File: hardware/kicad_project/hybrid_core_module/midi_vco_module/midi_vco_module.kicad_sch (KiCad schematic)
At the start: 14 parts, among them J1 AudioJack2_SwitchT, J2 Screw_Terminal_01x08, J3 AudioJack2_SwitchT, J4 AudioJack2_SwitchT, J5 AudioJack2_SwitchT, J6 AudioJack2_SwitchT, SW1 SW_Push, SW2 SW_Rotary_1x4_MP, SW3 SW_Rotary_1x4_MP

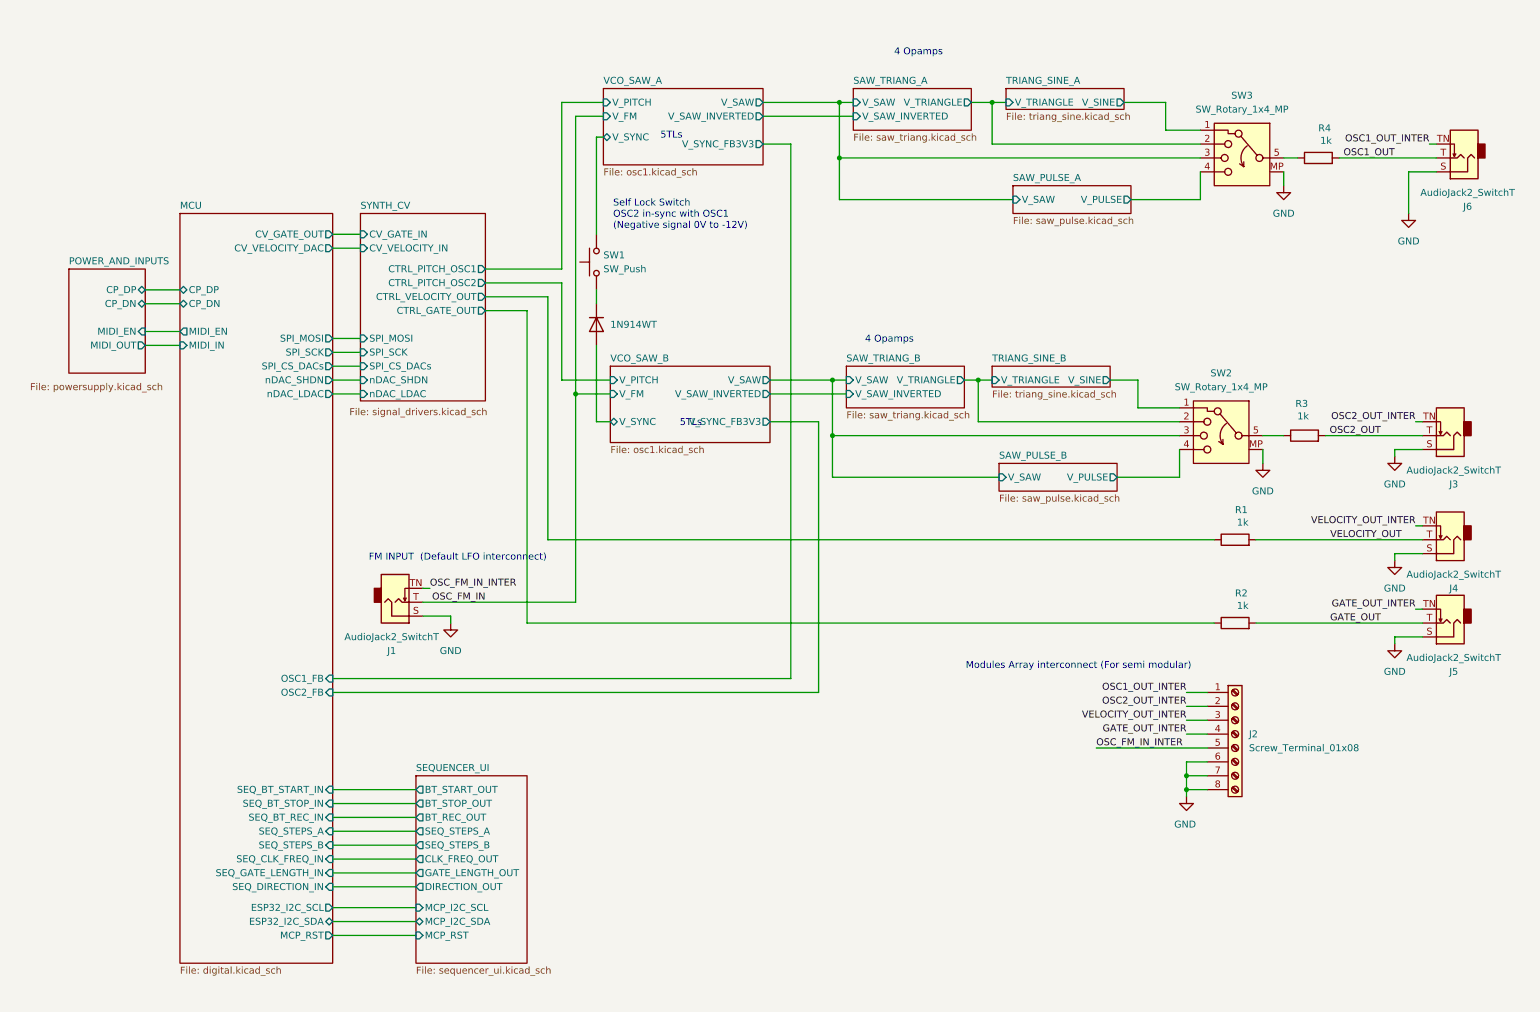
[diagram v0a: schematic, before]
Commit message: Schematic updated. Components Footprint assignment started. Waiting for components mechanical validation before starting layout.
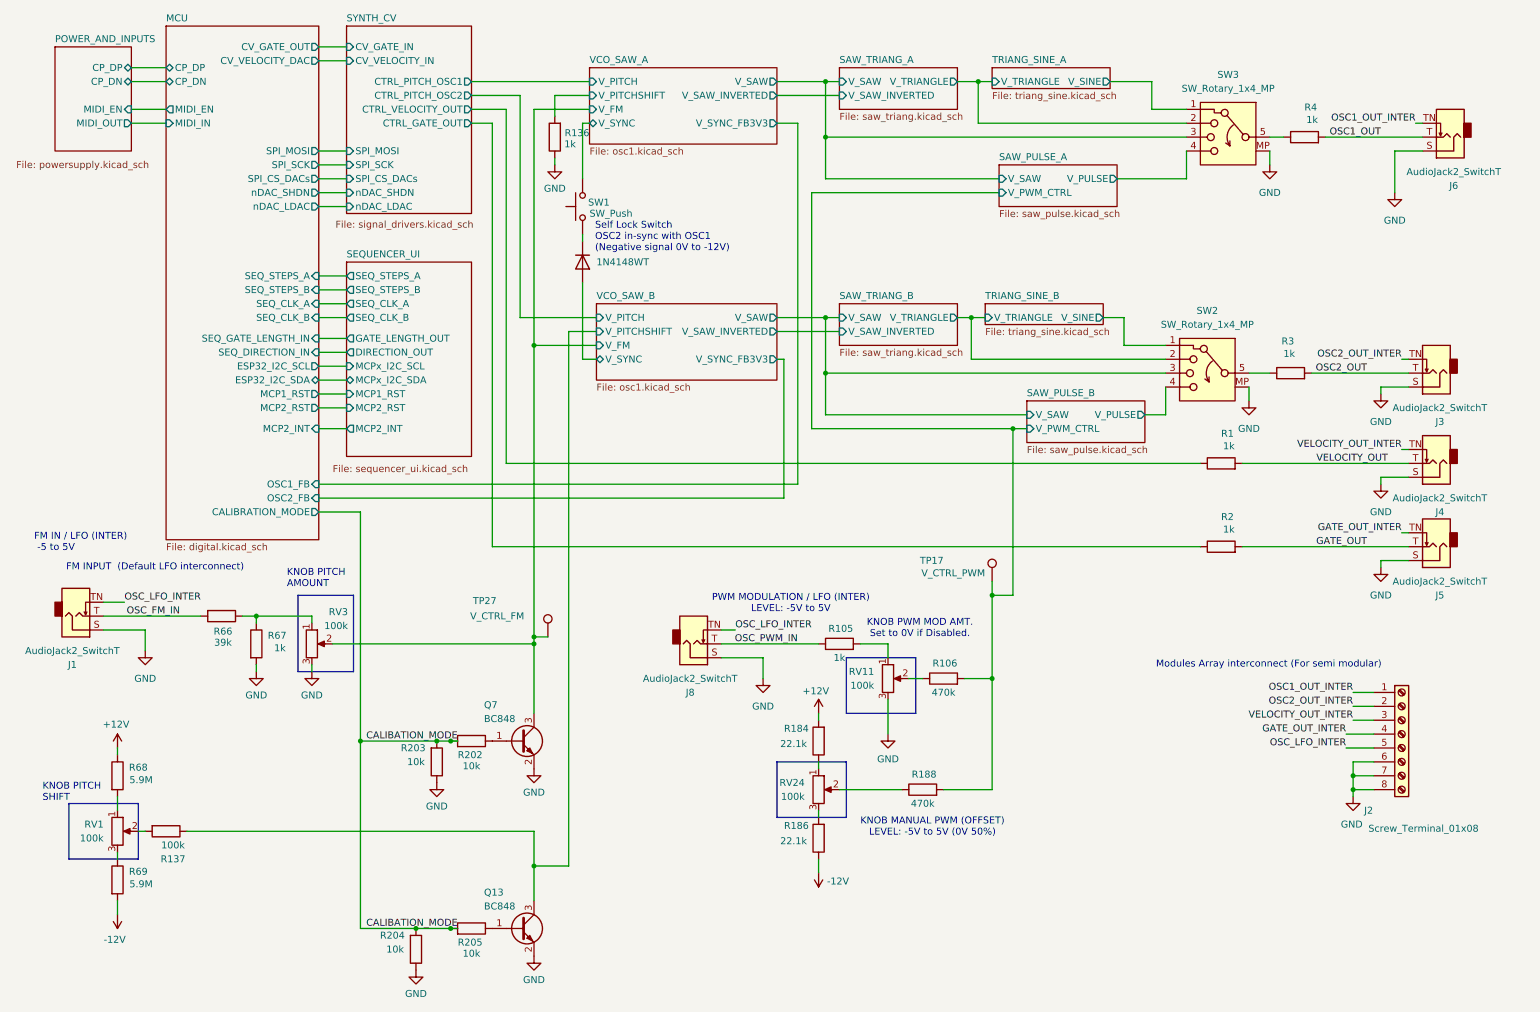
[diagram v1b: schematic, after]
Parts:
- added J8: AudioJack2_SwitchT, mylib:Jack_3.5mm_QingPu_WQP-PJ398SM_Vertical_CircularHoles, symbol Connector_Audio:AudioJack2_SwitchT
- added Q13, Q7: BC848, Package_TO_SOT_SMD:SOT-23, symbol Transistor_BJT:BC848
- added R105, R136, R67: 1k, Resistor_SMD:R_0402_1005Metric, symbol Device:R
- added R106, R188: 470k, Resistor_SMD:R_0402_1005Metric, symbol Device:R
- added R137: 100k, Resistor_SMD:R_0402_1005Metric, symbol Device:R
- added R184, R186: 22.1k, Resistor_SMD:R_0402_1005Metric, symbol Device:R
- added R202, R203, R204, R205: 10k, Resistor_SMD:R_0402_1005Metric, symbol Device:R
- added R66: 39k, Resistor_SMD:R_0402_1005Metric, symbol Device:R
- added R68, R69: 5.9M, Resistor_SMD:R_0402_1005Metric, symbol Device:R
- added RV1, RV11, RV24, RV3: 100k, symbol Device:R_Potentiometer
- added TP17: V_CTRL_PWM, symbol Connector:TestPoint
- added TP27: V_CTRL_FM, symbol Connector:TestPoint
- D1: value 1N914WT -> 1N4148WT; Manufacturer (none) -> ONSEMI/FAIRCHILD; Manufacturer PartNumer (none) -> 1N4148WT
- J1, J3, J4, J5, J6: footprint (none) -> mylib:Jack_3.5mm_QingPu_WQP-PJ398SM_Vertical_CircularHoles
- J2: footprint (none) -> TerminalBlock_CUI:TerminalBlock_CUI_TB007-508-08_1x08_P5.08mm_Horizontal; Manufacturer (none) -> Same Sky; Manufacturer PartNumer (none) -> TB007-508-08BE
- R1, R2, R3, R4: footprint (none) -> Resistor_SMD:R_0402_1005Metric; Manufacturer (none) -> YAGEO; Manufacturer PartNumer (none) -> RT0402FRE071KL
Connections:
- net GND: now also J8.S, Q13.2 (E), Q7.2 (E), R136.1, R203.1, R204.1, R67.2, RV11.3, RV3.3
- net OSC_FM_IN: now also R66.2
- net OSC_FM_IN_INTER renamed OSC_LFO_INTER
- net OSC_LFO_INTER: now also J8.TN
- new net: R186.2, RV24.3
- new net: R105.2, RV11.1
- new net: R106.1, RV11.2
- new net: R66.1, R67.1, RV3.1
- new net: R184.1, RV24.1
- new net: Q7.1 (B), R202.1
- new net: R68.2, RV1.1
- new net: R69.1, RV1.3
- new net: R137.2, RV1.2
- new net: Q13.1 (B), R205.1
- new net: R188.1, RV24.2
- new net +12V: R184.2, R68.1
- new net -12V: R186.1, R69.2
- new net CALIBATION_MODE: R202.2, R203.2, R204.2, R205.2
- new net OSC_PWM_IN: J8.T, R105.1
- new net SAW_PULSE_A/V_PWM_CTRL: R106.2, R188.2, TP17.1
- new net VCO_SAW_A/V_FM: Q7.3 (C), RV3.2, TP27.1
- new net VCO_SAW_A/V_PITCHSHIFT: R136.2
- new net VCO_SAW_B/V_PITCHSHIFT: Q13.3 (C), R137.1
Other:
- sheet MCU ports: added CALIBRATION_MODE, MCP1_RST, MCP2_INT, MCP2_RST, SEQ_CLK_A, SEQ_CLK_B; removed MCP_RST, SEQ_BT_REC_IN, SEQ_BT_START_IN, SEQ_BT_STOP_IN, SEQ_CLK_FREQ_IN
- sheet SAW_PULSE_A ports: added V_PWM_CTRL; removed none
- sheet SAW_PULSE_B ports: added V_PWM_CTRL; removed none
- sheet SEQUENCER_UI ports: added MCP1_RST, MCP2_INT, MCP2_RST, MCPx_I2C_SCL, MCPx_I2C_SDA, SEQ_CLK_A, SEQ_CLK_B; removed BT_REC_OUT, BT_START_OUT, BT_STOP_OUT, CLK_FREQ_OUT, MCP_I2C_SCL, MCP_I2C_SDA, MCP_RST
- sheet VCO_SAW_A ports: added V_PITCHSHIFT; removed none
- sheet VCO_SAW_B ports: added V_PITCHSHIFT; removed none
- note added: "FM IN / LFO (INTER) -5 to 5V"
- note added: "KNOB MANUAL PWM (OFFSET) LEVEL: -5V to 5V (0V 50%)"
- note added: "KNOB PITCH AMOUNT"
- note added: "KNOB PITCH SHIFT"
- note added: "KNOB PWM MOD AMT. Set to 0V if Disabled."
- note added: "PWM MODULATION / LFO (INTER) LEVEL: -5V to 5V"
- note removed: "4 Opamps"
- note removed: "5TLs"
- moved on the sheet: J1, J2, J3, J4, J5, J6, R1, R2, R3, R4, SW1, SW2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

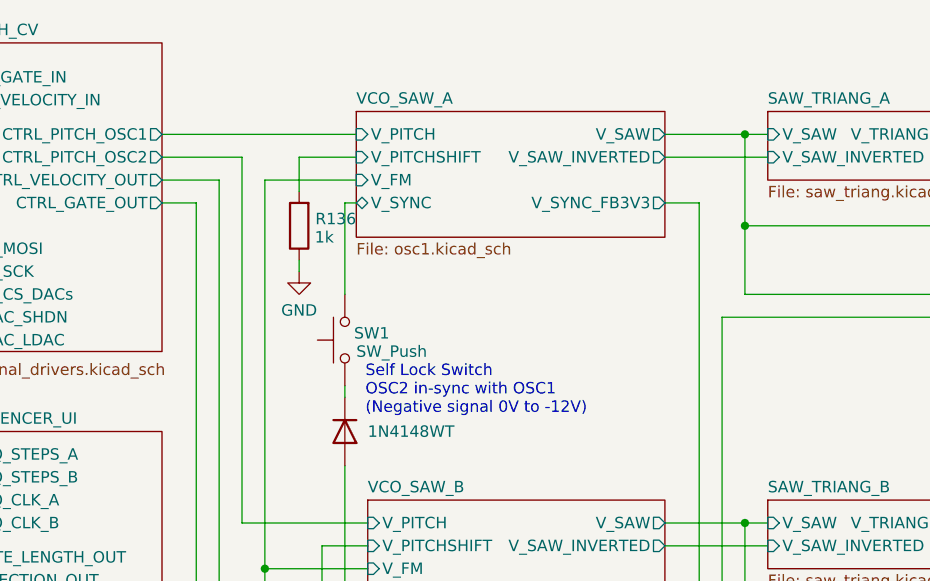
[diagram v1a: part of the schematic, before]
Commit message: - schematic updated  - PN and footprints added
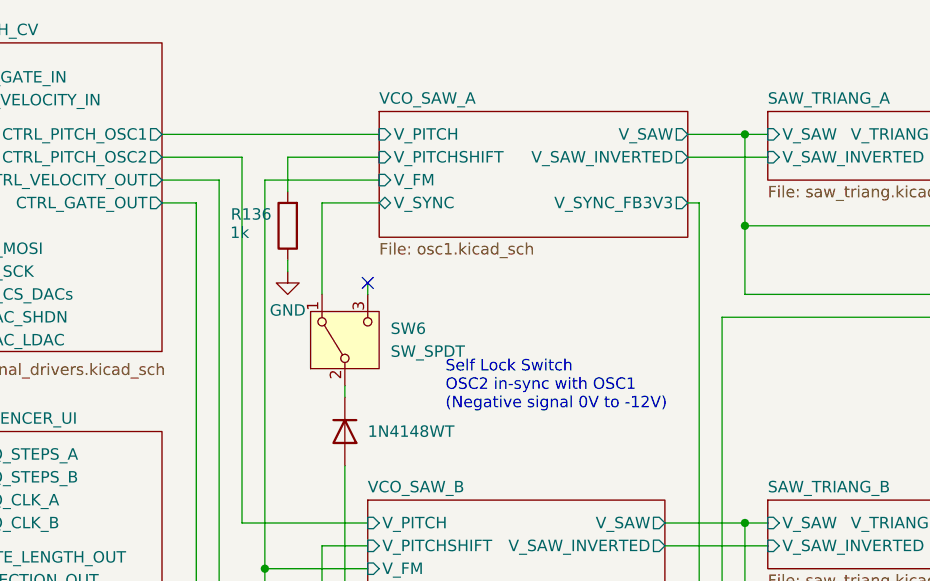
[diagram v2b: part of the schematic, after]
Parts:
- removed SW1: SW_Push, symbol Switch:SW_Push
- added SW6: SW_SPDT, mylib:SW_Toggle_Blue_wSlots, symbol Switch:SW_SPDT
- Q13, Q7: Manufacturer (none) -> Fairchild Semiconductor; Manufacturer PartNumer (none) -> BC848A
- RV1, RV11, RV24, RV3: footprint (none) -> Potentiometer_THT:Potentiometer_Bourns_3296W_Vertical; Manufacturer (none) -> KESHY; Manufacturer PartNumer (none) -> 3296W-104-LF
- SW2, SW3: footprint (none) -> mylib:SR16 Rotary Band Switch; Manufacturer (none) -> ALIEXPRESS; Manufacturer PartNumer (none) -> SR16
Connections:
- net VCO_SAW_A/V_SYNC: now also SW6.1 (A)
- net at D1.1 (K): now also SW6.2 (B)
- no-connect marks 0 -> 1
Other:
- moved on the sheet: R136

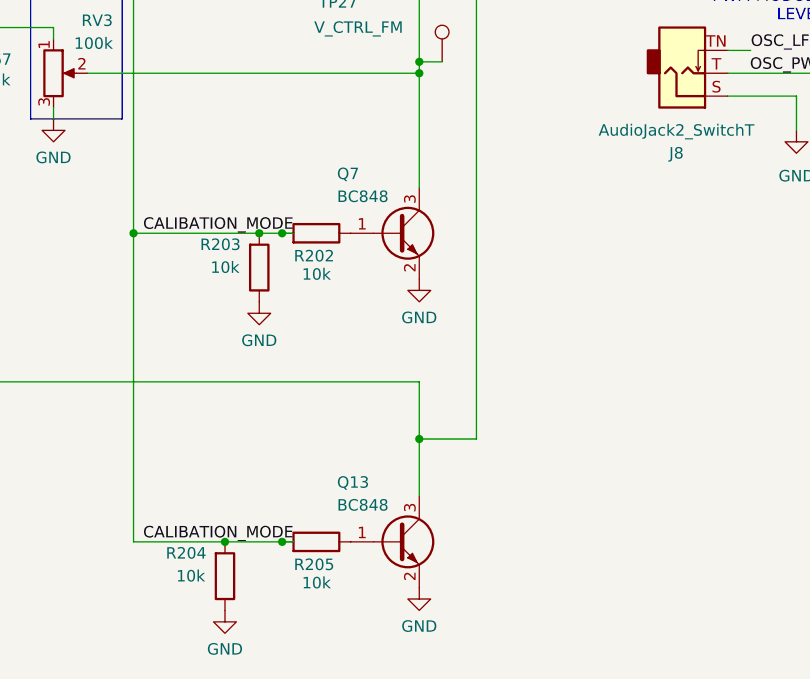
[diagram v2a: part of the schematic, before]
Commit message: components placement (interface) components placement per section
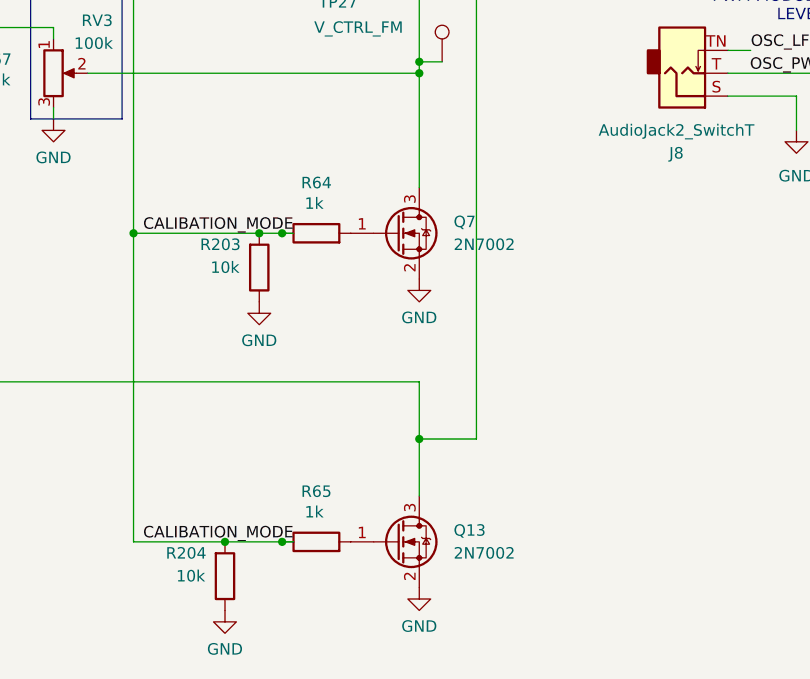
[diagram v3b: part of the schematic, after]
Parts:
- removed Q13, Q7: BC848, Package_TO_SOT_SMD:SOT-23, symbol Transistor_BJT:BC848
- removed R202, R205: 10k, Resistor_SMD:R_0402_1005Metric, symbol Device:R
- added Q13, Q7: 2N7002, Package_TO_SOT_SMD:SOT-23, symbol Transistor_FET:2N7002
- added R64, R65: 1k, Resistor_SMD:R_0402_1005Metric, symbol Device:R
- RV1, RV11, RV24, RV3: footprint Potentiometer_THT:Potentiometer_Bourns_3296W_Vertical -> mylib:Potentiometer_RV09_Single_Vertical
- TP17, TP27: footprint (none) -> TestPoint:TestPoint_Pad_1.0x1.0mm
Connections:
- net CALIBATION_MODE: now also R64.1, R65.1
- net GND: now also Q13.2 (S), Q7.2 (S)
- net VCO_SAW_A/V_FM: now also Q7.3 (D)
- net VCO_SAW_B/V_PITCHSHIFT: now also Q13.3 (D)
- new net: Q13.1 (G), R65.2
- new net: Q7.1 (G), R64.2

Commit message: - placement done - routing 60%
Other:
- sheet MCU ports: added CP_D_N, CP_D_P; removed CP_DN, CP_DP
- sheet POWER_AND_INPUTS ports: added CP_D_N, CP_D_P; removed CP_DN, CP_DP
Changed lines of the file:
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@@
-			)
-		)
-		(pin "CP_DP" bidirectional
-			(at 39.37 22.86 180)
-			(effects
-				(font
-					(size 1.27 1.27)
-				)
-				(justify left)
-			)
-		)
-		(pin "CP_DN" bidirectional
-			(at 39.37 25.4 180)
-			(effects
-				(font
-					(size 1.27 1.27)
-				)
-				(justify left)
 			)
 		)
@@
 				)
 				(justify right)
+			)
+		)
+		(pin "CP_D_P" bidirectional
+			(at 39.37 22.86 180)
+			(effects
+				(font
+					(size 1.27 1.27)
+				)
+				(justify left)
+			)
+		)
+		(pin "CP_D_N" bidirectional
+			(at 39.37 25.4 180)
+			(effects
+				(font
+					(size 1.27 1.27)
+				)
+				(justify left)
 			)
 		)
@@
 			)
 		)
-		(pin "CP_DN" bidirectional
-			(at 33.02 25.4 0)
-			(effects
-				(font
-					(size 1.27 1.27)
-				)
-				(justify right)
-			)
-		)
-		(pin "CP_DP" bidirectional
-			(at 33.02 22.86 0)
-			(effects
-				(font
-					(size 1.27 1.27)
-				)
-				(justify right)
-			)
-		)
 		(pin "MIDI_EN" input
 			(at 33.02 30.48 0)
@@
 			(effects
 				(font
+					(size 1.27 1.27)
+				)
+				(justify right)
+			)
+		)
+		(pin "CP_D_N" bidirectional
+			(at 33.02 25.4 0)
+			(effects
+				(font
+					(size 1.27 1.27)
+				)
+				(justify right)
+			)
+		)
+		(pin "CP_D_P" bidirectional
+			(at 33.02 22.86 0)
+			(effects
+				(font

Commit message: routing continued.
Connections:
- net GATE_OUT_INTER: now also J2.3 (Pin_3); no longer J2.4 (Pin_4)
- net VELOCITY_OUT_INTER: now also J2.4 (Pin_4); no longer J2.3 (Pin_3)
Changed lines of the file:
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@@
 	(wire
 		(pts
-			(xy 255.27 144.78) (xy 260.35 144.78)
+			(xy 256.54 144.78) (xy 260.35 144.78)
 		)
 		(stroke
@@
 	(wire
 		(pts
-			(xy 255.27 147.32) (xy 260.35 147.32)
+			(xy 256.54 147.32) (xy 260.35 147.32)
 		)
 		(stroke
@@
 		)
 	)
-	(label "OSC2_OUT_INTER"
-		(at 256.54 139.7 180)
-		(effects
-			(font
-				(size 1.27 1.27)
-			)
-			(justify right bottom)
-		)
-	)
 	(label "CALIBATION_MODE"
 		(at 92.71 180.34 180)
@@
 	)
 	(label "VELOCITY_OUT_INTER"
+		(at 256.54 144.78 180)
+		(effects
+			(font
+				(size 1.27 1.27)
+			)
+			(justify right bottom)
+		)
+	)
+	(label "VELOCITY_OUT_INTER"
 		(at 265.43 92.71 180)
 		(effects
@@
 		)
 	)
-	(label "OSC_LFO_INTER"
-		(at 255.27 147.32 180)
+	(label "OSC2_OUT_INTER"
+		(at 256.54 139.7 180)
 		(effects
 			(font
@@
 		)
 	)
-	(label "VELOCITY_OUT_INTER"
-		(at 256.54 142.24 180)
-		(effects
-			(font
-				(size 1.27 1.27)
-			)
-			(justify right bottom)
-		)
-	)
 	(label "VELOCITY_OUT"
 		(at 262.89 95.25 180)
@@
 		)
 	)
-	(label "GATE_OUT"
-		(at 259.08 110.49 180)
+	(label "OSC_LFO_INTER"
+		(at 256.54 147.32 180)
 		(effects
 			(font
@@
 		)
 	)
-	(label "OSC1_OUT_INTER"
-		(at 267.97 33.02 180)
+	(label "GATE_OUT_INTER"
+		(at 256.54 142.24 180)
 		(effects
 			(font
@@
 		)
 	)
-	(label "GATE_OUT_INTER"
-		(at 255.27 144.78 180)
+	(label "GATE_OUT"
+		(at 259.08 110.49 180)
+		(effects
+			(font
+				(size 1.27 1.27)
+			)
+			(justify right bottom)
+		)
+	)
+	(label "OSC1_OUT_INTER"
+		(at 267.97 33.02 180)
 		(effects
 			(font
@@
 		)
 		(instances
-			(project ""
+			(project "midi_vco_module"
 				(path "/3378c2b5-f4b3-47f0-8cdf-dba4991b82b5"
 					(reference "J2")
